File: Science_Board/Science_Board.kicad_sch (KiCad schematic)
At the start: 36 parts, among them J1 Conn_01x02, J10 Conn_01x02, J11 Conn_01x03, J12 Conn_01x03, J13 Conn_01x03, J14 Conn_01x03, J15 Conn_01x03, J16 Conn_01x03, J17 Conn_01x03, J18 Conn_01x03, J19 Conn_01x02, J2 RJ45_LED_Shielded, J20 Molex_Megafit_02, J23 Conn_01x02, J5 Conn_01x05, J6 Conn_01x04, J7 Conn_01x03, J8 Conn_01x03, J9 Conn_01x02, Q5 NMOS, U5 PCA9685BS

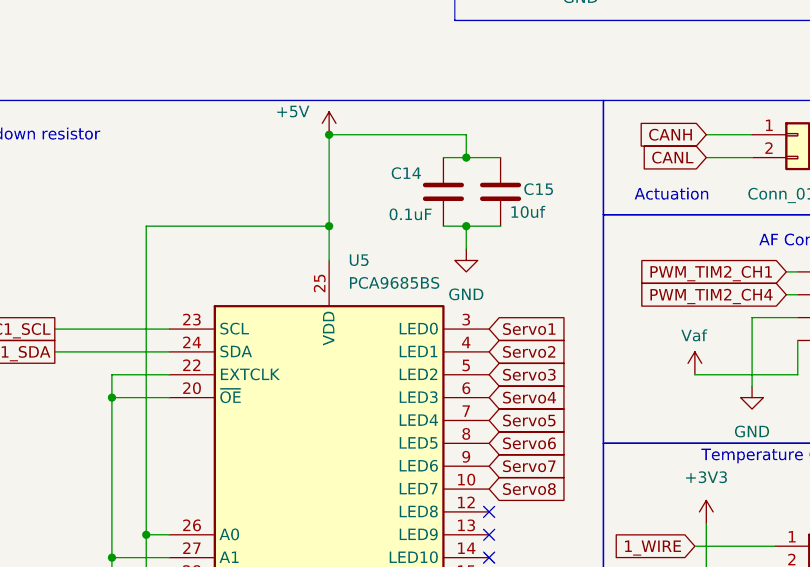
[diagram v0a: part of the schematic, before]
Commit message: fixed pwm driver and a connecter footprint
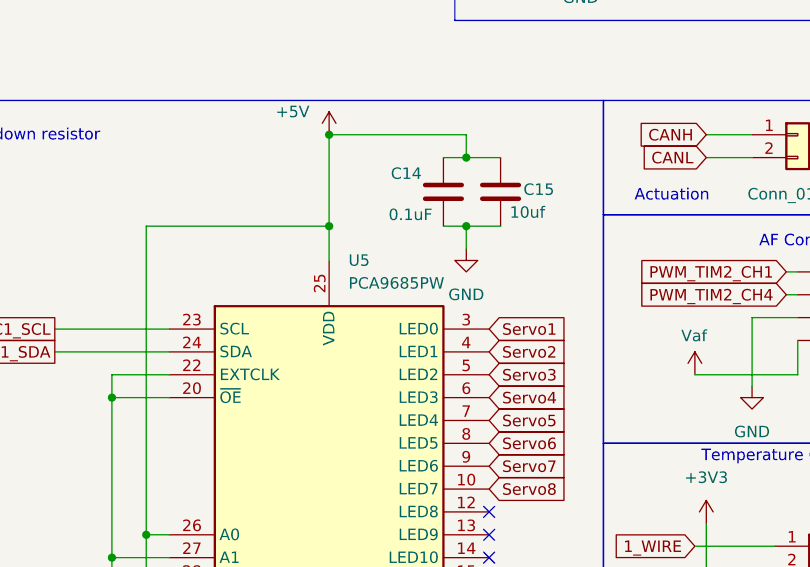
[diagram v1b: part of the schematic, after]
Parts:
- J5: footprint Package_DFN_QFN:QFN-20-1EP_5x5mm_P0.65mm_EP3.35x3.35mm -> Connector_JST:JST_PH_B5B-PH-K_1x05_P2.00mm_Vertical
- U5: value PCA9685BS -> PCA9685PW; footprint Package_DFN_QFN:QFN-28-1EP_6x6mm_P0.65mm_EP4.25x4.25mm -> Package_SO:HTSSOP-28-1EP_4.4x9.7mm_P0.65mm_EP2.75x6.2mm
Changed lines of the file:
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@@
 			)
 		)
-		(property "Footprint" "Package_DFN_QFN:QFN-20-1EP_5x5mm_P0.65mm_EP3.35x3.35mm"
+		(property "Footprint" "Connector_JST:JST_PH_B5B-PH-K_1x05_P2.00mm_Vertical"
 			(at 218.44 106.68 0)
 			(hide yes)
@@
 			)
 		)
-		(property "Value" "PCA9685BS"
+		(property "Value" "PCA9685PW"
 			(at 105.0133 121.92 0)
 			(show_name no)
@@
 			)
 		)
-		(property "Footprint" "Package_DFN_QFN:QFN-28-1EP_6x6mm_P0.65mm_EP4.25x4.25mm"
+		(property "Footprint" "Package_SO:HTSSOP-28-1EP_4.4x9.7mm_P0.65mm_EP2.75x6.2mm"
 			(at 103.505 169.545 0)
 			(hide yes)

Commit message: fixed the 1wire pin
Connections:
- net 1_WIRE: now also U2.17 (PB14); no longer U2.35 (PH1)
- net AF_EN: now also U2.12 (PA8); no longer U2.17 (PB14)
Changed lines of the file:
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@@
 	)
 	(no_connect
-		(at 246.38 55.88)
-	)
-	(no_connect
 		(at 222.25 49.53)
 	)
@@
 	)
 	(no_connect
+		(at 222.25 52.07)
+	)
+	(no_connect
 		(at 120.65 149.86)
 	)
@@
 	(wire
 		(pts
+			(xy 246.38 55.88) (xy 247.65 55.88)
+		)
+		(stroke
+			(width 0)
+			(type default)
+		)
+	)
+	(wire
+		(pts
 			(xy 222.25 158.75) (xy 199.39 158.75)
 		)
@@
 	(wire
 		(pts
-			(xy 214.63 52.07) (xy 222.25 52.07)
-		)
-		(stroke
-			(width 0)
-			(type default)
-		)
-	)
-	(wire
-		(pts
 			(xy 175.26 111.76) (xy 180.34 111.76)
 		)
@@
 		)
 	)
+	(global_label "1_WIRE"
+		(shape input)
+		(at 247.65 68.58 0)
+		(fields_autoplaced yes)
+		(effects
+			(font
+				(size 1.27 1.27)
+			)
+			(justify left)
+		)
+		(property "Intersheetrefs" "${INTERSHEET_REFS}"
+			(at 257.2875 68.58 0)
+			(hide yes)
+			(show_name no)
+			(do_not_autoplace no)
+			(effects
+				(font
+					(size 1.27 1.27)
+				)
+				(justify left)
+			)
+		)
+	)
 	(global_label "Servo8"
 		(shape input)
@@
 		)
 	)
-	(global_label "AF_EN"
-		(shape output)
-		(at 247.65 68.58 0)
-		(fields_autoplaced yes)
-		(effects
-			(font
-				(size 1.27 1.27)
-				(thickness 0.1588)
-			)
-			(justify left)
-		)
-		(property "Intersheetrefs" "${INTERSHEET_REFS}"
-			(at 256.2595 68.58 0)
-			(hide yes)
-			(show_name no)
-			(do_not_autoplace no)
-			(effects
-				(font
-					(size 1.27 1.27)
-				)
-				(justify left)
-			)
-		)
-	)
 	(global_label "I2C1_SDA"
 		(shape input)
@@
 		)
 	)
+	(global_label "AF_EN"
+		(shape output)
+		(at 247.65 55.88 0)
+		(fields_autoplaced yes)
+		(effects
+			(font
+				(size 1.27 1.27)
+				(thickness 0.1588)
+			)
+			(justify left)
+		)
+		(property "Intersheetrefs" "${INTERSHEET_REFS}"
+			(at 256.2595 55.88 0)
+			(hide yes)
+			(show_name no)
+			(do_not_autoplace no)
+			(effects
+				(font
+					(size 1.27 1.27)
+				)
+				(justify left)
+			)
+		)
+	)
 	(global_label "Servo1"
 		(shape input)
@@
 			(hide yes)
 			(show_name no)
-			(do_not_autoplace no)
-			(effects
-				(font
-					(size 1.27 1.27)
-				)
-				(justify right)
-			)
-		)
-	)
-	(global_label "1_WIRE"
-		(shape input)
-		(at 214.63 52.07 180)
-		(fields_autoplaced yes)
-		(effects
-			(font
-				(size 1.27 1.27)
-			)
-			(justify right)
-		)
-		(property "Intersheetrefs" "${INTERSHEET_REFS}"
-			(at 204.9925 52.07 0)
-			(hide yes)
-			(show_name no)

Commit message: Working on compacting layout
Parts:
- J2: footprint Connector_RJ:RJ45_Amphenol_RJMG1BD3B8K1ANR -> MRDT_Connectors:RJ45_Teensy
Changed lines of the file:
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@@
 			)
 		)
-		(property "Footprint" "Connector_RJ:RJ45_Amphenol_RJMG1BD3B8K1ANR"
+		(property "Footprint" "MRDT_Connectors:RJ45_Teensy"
 			(at 199.39 141.605 90)
 			(hide yes)

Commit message: added temp connector =
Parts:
- added J24: Conn_01x02, Connector_JST:JST_PH_B2B-PH-K_1x02_P2.00mm_Vertical, symbol Connector_Generic:Conn_01x02
- added Q6: NMOS, Package_TO_SOT_SMD:SOT-23-3, symbol Simulation_SPICE:NMOS
- added R48: 100, Resistor_THT:R_Array_SIP4, symbol Device:R_US
- added R49: 10k, Resistor_THT:R_Array_SIP4, symbol Device:R_US
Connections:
- net +5V: now also J24.1 (Pin_1)
- net +PV: no longer J20.1
- net GND: now also Q6.3 (S), R49.1
- net TEMP_CONTROL: now reaches U2.42 (PB0)
- net TEMP_CONTROL: now also R48.1, R49.2
- new net: J24.2 (Pin_2), Q6.1 (D)
- new net: Q6.2 (G), R48.2
- new net +Vpre: J20.1
- no-connect marks 15 -> 14
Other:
- note added: "Heater"

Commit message: fixed footprint
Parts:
- R48, R49: footprint Resistor_THT:R_Array_SIP4 -> Resistor_SMD:R_0603_1608Metric_Pad0.98x0.95mm_HandSolder
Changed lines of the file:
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@@
 			)
 		)
-		(property "Footprint" "Resistor_THT:R_Array_SIP4"
+		(property "Footprint" "Resistor_SMD:R_0603_1608Metric_Pad0.98x0.95mm_HandSolder"
 			(at 75.184 93.726 90)
 			(hide yes)
@@
 			)
 		)
-		(property "Footprint" "Resistor_THT:R_Array_SIP4"
+		(property "Footprint" "Resistor_SMD:R_0603_1608Metric_Pad0.98x0.95mm_HandSolder"
 			(at 84.074 87.884 90)
 			(hide yes)
